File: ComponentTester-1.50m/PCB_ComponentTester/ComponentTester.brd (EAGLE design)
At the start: 68.6 x 53.3 mm, 76 parts, among them U1 ATMEGA328P-AU

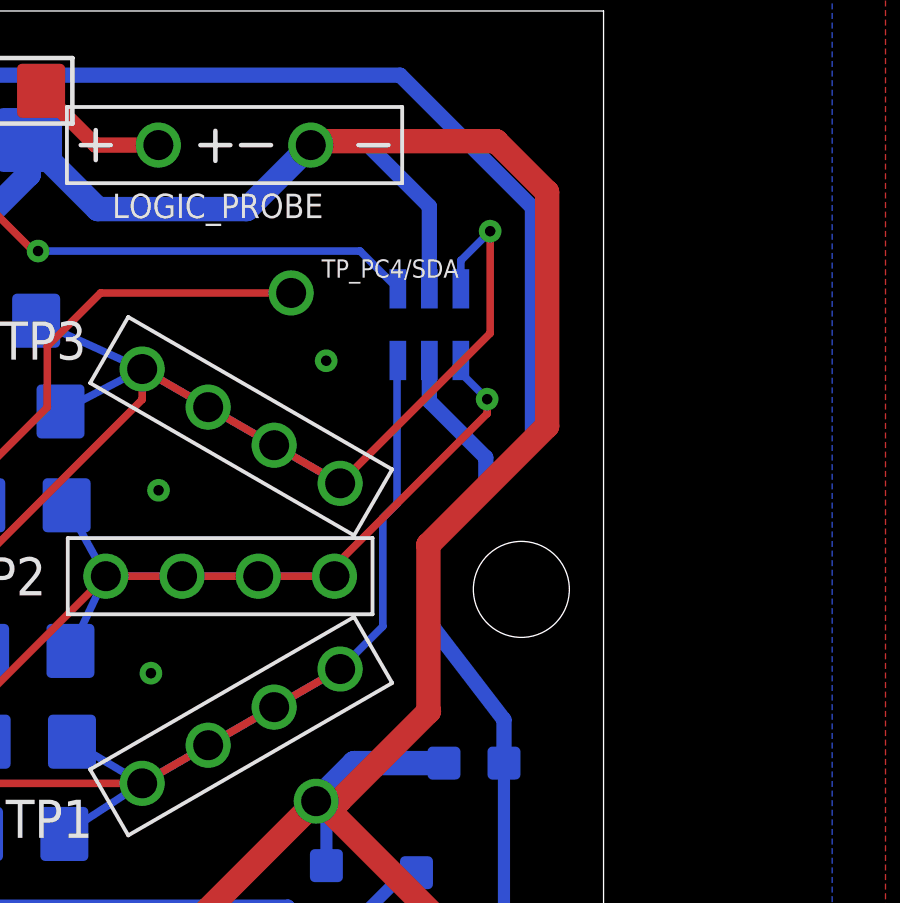
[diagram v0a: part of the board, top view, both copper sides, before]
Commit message: Mounting Hole correction on PCB
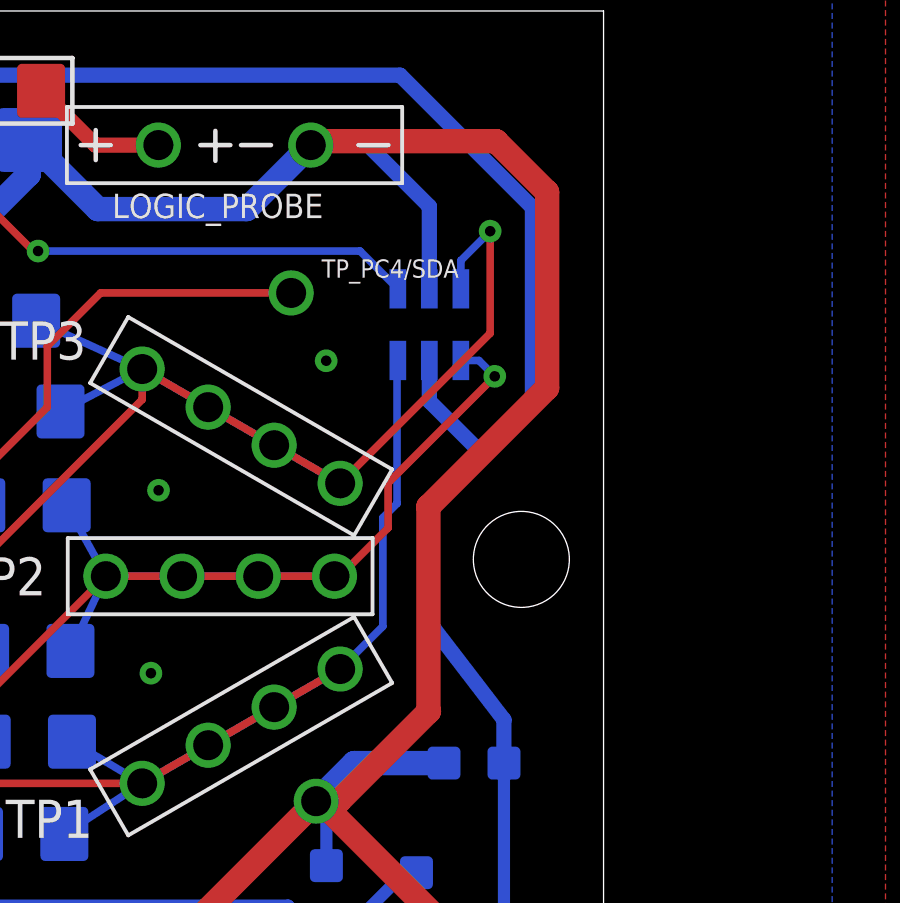
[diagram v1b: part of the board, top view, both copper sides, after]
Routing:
- net 5V: track 219.2 -> 218.0 mm
- net TP2: track 45.0 -> 45.7 mm
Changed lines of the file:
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@@
 <setting verticaltext="up"/>
 </settings>
-<grid distance="10" unitdist="mil" unit="mil" style="lines" multiple="1" display="yes" altdistance="1" altunitdist="mil" altunit="mil"/>
+<grid distance="10" unitdist="mil" unit="mm" style="lines" multiple="1" display="yes" altdistance="1" altunitdist="mil" altunit="mil"/>
 <layers>
 <layer number="1" name="Top" color="4" fill="1" visible="yes" active="yes"/>
@@
 <layer number="43" name="vRestrict" color="2" fill="10" visible="no" active="yes"/>
 <layer number="44" name="Drills" color="7" fill="1" visible="no" active="yes"/>
-<layer number="45" name="Holes" color="7" fill="1" visible="no" active="yes"/>
+<layer number="45" name="Holes" color="7" fill="1" visible="yes" active="yes"/>
 <layer number="46" name="Milling" color="3" fill="1" visible="no" active="yes"/>
 <layer number="47" name="Measures" color="7" fill="1" visible="no" active="yes"/>
@@
 <hole x="13.97" y="2.54" drill="3.2"/>
 <hole x="66.04" y="7.62" drill="3.2"/>
-<hole x="65.84" y="34.06" drill="3.2"/>
+<hole x="65.84" y="35.06" drill="3.2"/>
 <hole x="15.24" y="50.8" drill="3.2"/>
 <text x="19.05" y="1.524" size="1.6764" layer="21">ULTIMATE TESTER :)</text>
@@
 <wire x1="58.95" y1="49" x2="65" y2="49" width="0.8128" layer="1"/>
 <wire x1="65" y1="49" x2="66.7" y2="47.3" width="0.8128" layer="1"/>
-<wire x1="66.7" y1="47.3" x2="66.7" y2="39.506925" width="0.8128" layer="1"/>
-<wire x1="66.7" y1="39.506925" x2="62.7414" y2="35.548325" width="0.8128" layer="1"/>
-<wire x1="62.7414" y1="35.548325" x2="62.7414" y2="29.9972" width="0.8128" layer="1"/>
+<wire x1="66.7" y1="47.3" x2="66.7" y2="40.776925" width="0.8128" layer="1"/>
+<wire x1="66.7" y1="40.776925" x2="62.7414" y2="36.818325" width="0.8128" layer="1"/>
+<wire x1="62.7414" y1="36.818325" x2="62.7414" y2="29.9972" width="0.8128" layer="1"/>
 <wire x1="62.7414" y1="29.9972" x2="62.7592" y2="29.9972" width="0.8128" layer="1"/>
 <wire x1="62.7592" y1="29.9972" x2="59.762" y2="27" width="0.8128" layer="1"/>
@@
 <wire x1="57.07" y1="34.5" x2="54.53" y2="34.5" width="0.254" layer="1"/>
 <wire x1="54.53" y1="34.5" x2="51.99" y2="34.5" width="0.254" layer="1"/>
-<wire x1="63.8228" y1="41.6908" x2="63.8228" y2="41.2772" width="0.254" layer="16"/>
-<wire x1="64.7" y1="40.4" x2="63.8228" y2="41.2772" width="0.254" layer="16"/>
-<via x="64.7" y="40.4" extent="1-16" drill="0.35"/>
-<wire x1="64.7" y1="40.4" x2="64.7" y2="39.9202" width="0.254" layer="1"/>
-<wire x1="64.7" y1="39.9202" x2="59.61" y2="34.8302" width="0.254" layer="1"/>
-<wire x1="59.61" y1="34.8302" x2="59.61" y2="34.5" width="0.254" layer="1"/>
+<wire x1="64.954" y1="41.162" x2="64.4252" y2="41.6908" width="0.254" layer="16"/>
+<wire x1="63.8228" y1="41.6908" x2="64.4252" y2="41.6908" width="0.254" layer="16"/>
+<via x="64.954" y="41.162" extent="1-16" drill="0.35"/>
+<wire x1="64.954" y1="41.162" x2="61.398" y2="37.606" width="0.254" layer="1"/>
+<wire x1="61.398" y1="37.606" x2="61.398" y2="36.1102" width="0.254" layer="1"/>
+<wire x1="61.398" y1="36.1102" x2="59.7878" y2="34.5" width="0.254" layer="1"/>
+<wire x1="59.61" y1="34.5" x2="59.7878" y2="34.5" width="0.254" layer="1"/>
 <wire x1="41.64" y1="32.06" x2="43.008" y2="30.692" width="0.254" layer="1"/>
 <wire x1="43.008" y1="30.692" x2="48.182" y2="30.692" width="0.254" layer="1"/>
@@
 <wire x1="43.516" y1="49.04" x2="45.04" y2="49.04" width="0.8128" layer="16"/>
 <wire x1="66.21" y1="46.79" x2="61.8" y2="51.2" width="0.508" layer="16"/>
-<wire x1="62.7728" y1="40.3372" x2="64.655" y2="38.455" width="0.508" layer="16"/>
+<wire x1="62.7728" y1="40.3372" x2="64.547" y2="38.563" width="0.508" layer="16"/>
 <wire x1="61.8" y1="51.2" x2="47.2" y2="51.2" width="0.508" layer="16"/>
 <wire x1="45.04" y1="49.04" x2="47.2" y2="51.2" width="0.508" layer="16"/>
-<wire x1="64.655" y1="37.655" x2="66.21" y2="39.21" width="0.508" layer="16"/>
-<wire x1="66.21" y1="39.21" x2="66.21" y2="46.79" width="0.508" layer="16"/>
+<wire x1="64.655" y1="38.709" x2="66.21" y2="40.264" width="0.508" layer="16"/>
+<wire x1="66.21" y1="40.264" x2="66.21" y2="46.79" width="0.508" layer="16"/>
 <wire x1="62.7728" y1="41.6908" x2="62.7728" y2="40.3372" width="0.508" layer="16"/>
-<wire x1="64.655" y1="38.455" x2="64.655" y2="37.655" width="0.508" layer="16"/>
-<wire x1="64.655" y1="37.655" x2="62.67" y2="35.67" width="0.508" layer="16"/>
+<wire x1="64.547" y1="38.563" x2="62.67" y2="36.686" width="0.508" layer="16"/>
 <wire x1="65.26" y1="28.27" x2="65.26" y2="29.71285625" width="0.508" layer="16"/>
 <wire x1="65.26" y1="29.71285625" x2="62.67" y2="33.08910625" width="0.508" layer="16"/>
-<wire x1="62.67" y1="35.67" x2="62.67" y2="33.08910625" width="0.508" layer="16"/>
+<wire x1="62.67" y1="36.686" x2="62.67" y2="33.08910625" width="0.508" layer="16"/>
 <wire x1="35.71785625" y1="41.54574375" x2="35.0651" y2="42.1985" width="0.508" layer="1"/>
 <contactref element="5V-LDO" pad="5"/>
